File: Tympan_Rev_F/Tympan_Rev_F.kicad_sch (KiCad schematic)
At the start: 89 parts, among them J1 SJ-3523-SMT-TR, J2 SJ-3524-SMT-TR-PI, J3 Conn_01x06, J4 Qwiik Connector, J7 J-Link, P1 CONN_01X06, P2 CONN_01X06, P3 CONN_01X06, P4 CONN_01X06, P6 CONN_01X01, P7 CONN_01X01, P8 CONN_01X01, SW1 CL-SB-22A, SW2 SW_Push, U1 MCP73831, U2 TLV320AIC3206IRSBT, U3 74LVC1G66, U4 LP5907MFX-1.8, U5 Teensy4.1, U6 LC709203, U7 MDBT50Q-1MV2, Y1 32.768

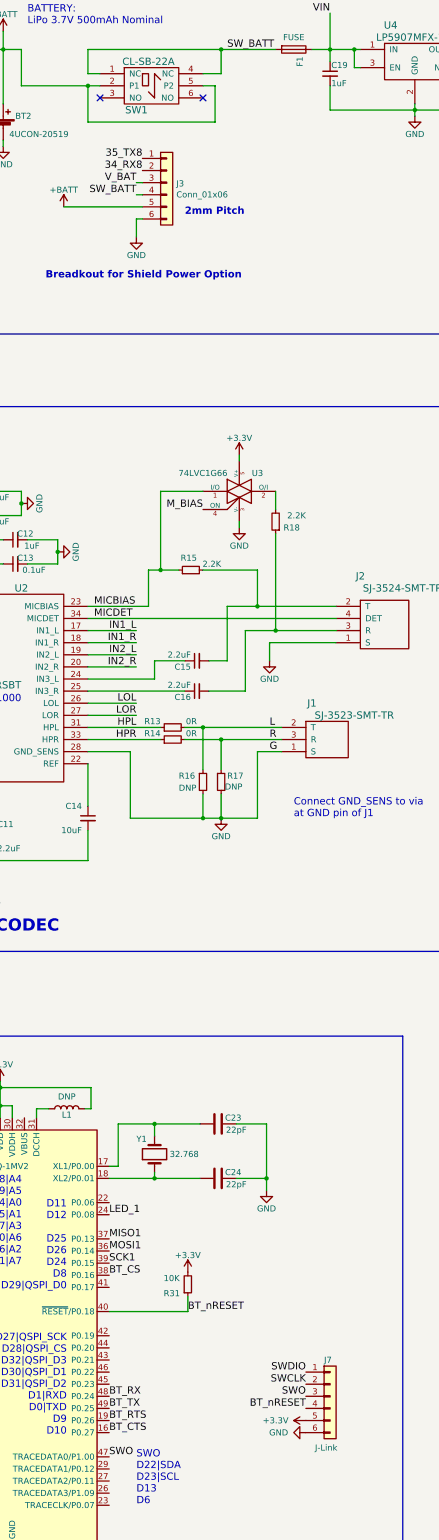
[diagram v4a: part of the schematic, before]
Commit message: first pass at laying out the J-Link interface
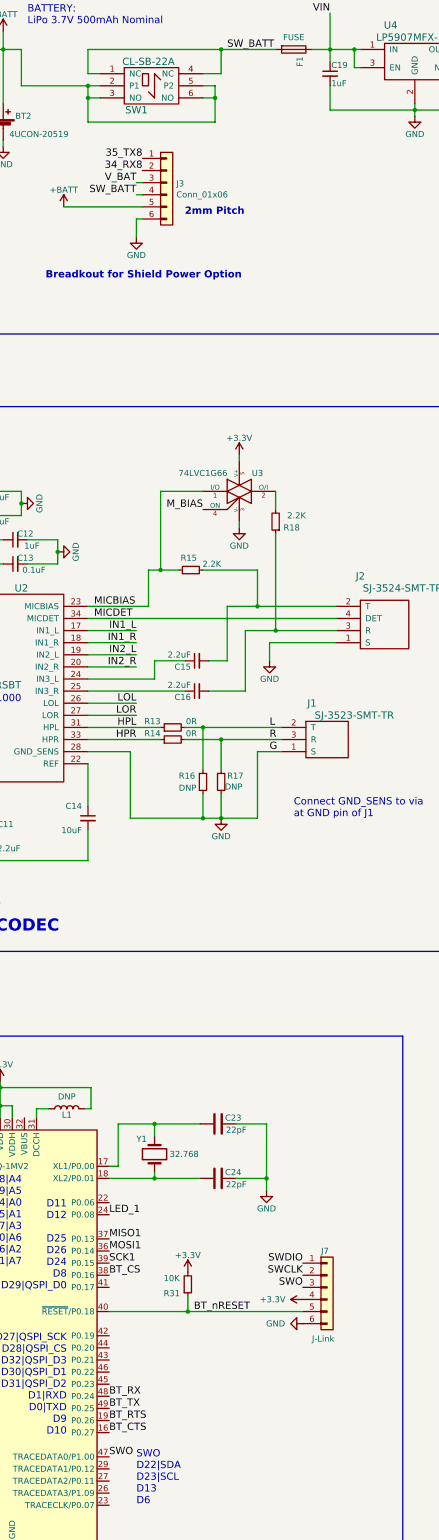
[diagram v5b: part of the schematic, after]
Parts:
- J7: footprint Connector_PinHeader_2.54mm:PinHeader_2x03_P2.54mm_Vertical_SMD -> Solutions:J-Link_SMT_SIP_0.1inP
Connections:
- net +3.3V: now also J7.4 (Pin_4); no longer J7.5 (Pin_5)
- net +BATT: now also SW1.3 (NO), SW1.6 (NO)
- net BT_nRESET: now also J7.5 (Pin_5); no longer J7.4 (Pin_4)
- no-connect marks 4 -> 2
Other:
- moved on the sheet: J7
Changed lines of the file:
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@@
     (rev "v1")
     (company "Tympan Master Hearing Aid Project")
-    (comment 1 "Designed by Flywheel Lab, Brooklyn")
+    (comment 1 "Designed by Flywheel Lab, Troy")
   )
   (junction (at 109.22 215.9) (diameter 0) (color 0 0 0 0)
@@
   (junction (at 189.23 54.61) (diameter 0) (color 0 0 0 0)
   )
+  (junction (at 160.02 64.77) (diameter 0) (color 0 0 0 0)
+  )
   (junction (at 261.62 152.4) (diameter 0) (color 0 0 0 0)
   )
@@
   (junction (at 114.935 276.225) (diameter 0) (color 0 0 0 0)
   )
+  (junction (at 133.35 64.77) (diameter 0) (color 0 0 0 0)
+  )
   (junction (at 114.935 272.415) (diameter 0) (color 0 0 0 0)
   )
@@
   (junction (at 96.52 142.24) (diameter 0) (color 0 0 0 0)
   )
+  (junction (at 154.305 319.405) (diameter 0) (color 0 0 0 0)
+  )
   (junction (at 219.71 54.61) (diameter 0) (color 0 0 0 0)
   )
@@
   )
   (no_connect (at 288.29 196.85))
-  (no_connect (at 157.48 64.77))
   (no_connect (at 288.29 162.56))
-  (no_connect (at 135.89 64.77))
   (wire (pts (xy 97.79 213.36) (xy 97.79 215.9))
     (stroke (width 0) (type default))
@@
     (stroke (width 0) (type default))
   )
-  (wire (pts (xy 133.35 62.23) (xy 133.35 69.85))
+  (wire (pts (xy 133.35 62.23) (xy 133.35 64.77))
     (stroke (width 0) (type default))
   )
@@
     (stroke (width 0) (type default))
   )
-  (wire (pts (xy 160.02 62.23) (xy 160.02 69.85))
+  (wire (pts (xy 160.02 62.23) (xy 160.02 64.77))
     (stroke (width 0) (type default))
   )
@@
     (stroke (width 0) (type default))
   )
+  (wire (pts (xy 133.35 64.77) (xy 135.89 64.77))
+    (stroke (width 0) (type default))
+  )
   (wire (pts (xy 261.62 190.5) (xy 264.16 190.5))
     (stroke (width 0) (type default))
@@
     (stroke (width 0) (type default))
   )
+  (wire (pts (xy 160.02 64.77) (xy 160.02 69.85))
+    (stroke (width 0) (type default))
+  )
+  (wire (pts (xy 157.48 64.77) (xy 160.02 64.77))
+    (stroke (width 0) (type default))
+  )
   (wire (pts (xy 426.085 150.495) (xy 445.135 150.495))
     (stroke (width 0) (type default))
@@
     (stroke (width 0) (type default))
   )
+  (wire (pts (xy 133.35 64.77) (xy 133.35 69.85))
+    (stroke (width 0) (type default))
+  )
   (wire (pts (xy 262.89 59.69) (xy 262.89 60.96))
     (stroke (width 0) (type default))
@@
     (stroke (width 0) (type default))
   )
+  (wire (pts (xy 137.795 319.405) (xy 154.305 319.405))
+    (stroke (width 0) (type default))
+  )
   (polyline (pts (xy 234.95 31.75) (xy 31.75 31.75))
     (stroke (width 0) (type default))
@@
     (stroke (width 0) (type default))
   )
-  (wire (pts (xy 137.795 319.405) (xy 154.305 319.405))
-    (stroke (width 0) (type default))
-  )
   (wire (pts (xy 164.465 280.035) (xy 170.815 280.035))
     (stroke (width 0) (type default))
@@
     (stroke (width 0) (type default))
   )
+  (wire (pts (xy 154.305 319.405) (xy 178.435 319.405))
+    (stroke (width 0) (type default))
+  )
   (wire (pts (xy 77.47 201.93) (xy 69.85 201.93))
     (stroke (width 0) (type default))
@@
     (effects (font (size 1.524 1.524)) (justify right bottom))
   )
-  (label "SWO" (at 179.07 337.185 180) (fields_autoplaced)
+  (label "SWO" (at 178.435 314.325 180) (fields_autoplaced)
     (effects (font (size 1.524 1.524)) (justify right bottom))
   )
-  (label "SWDIO" (at 179.07 332.105 180) (fields_autoplaced)
+  (label "SWDIO" (at 178.435 309.245 180) (fields_autoplaced)
     (effects (font (size 1.524 1.524)) (justify right bottom))
   )
@@
     (effects (font (size 1.524 1.524)) (justify right bottom))
   )
-  (label "SWCLK" (at 179.07 334.645 180) (fields_autoplaced)
+  (label "SWCLK" (at 178.435 311.785 180) (fields_autoplaced)
     (effects (font (size 1.524 1.524)) (justify right bottom))
   )
@@
     (effects (font (size 1.524 1.524)) (justify left bottom))
   )
-  (label "BT_nRESET" (at 154.305 319.405 0) (fields_autoplaced)
+  (label "BT_nRESET" (at 155.575 319.405 0) (fields_autoplaced)
     (effects (font (size 1.524 1.524)) (justify left bottom))
   )
@@
     (effects (font (size 1.524 1.524)) (justify left bottom))
   )
-  (label "BT_nRESET" (at 179.07 339.725 180) (fields_autoplaced)
-    (effects (font (size 1.524 1.524)) (justify right bottom))
-  )
   (label "SDA" (at 450.215 78.105 0) (fields_autoplaced)
     (effects (font (size 1.524 1.524)) (justify left bottom))
@@
     )
   )
-  (symbol (lib_id "power:GND") (at 179.07 344.805 270) (unit 1)
+  (symbol (lib_id "power:GND") (at 178.435 321.945 270) (unit 1)
     (in_bom yes) (on_board yes) (dnp no)
-    (property "Reference" "#PWR04" (at 172.72 344.805 0)
+    (property "Reference" "#PWR04" (at 172.085 321.945 0)
       (effects (font (size 1.27 1.27)) hide)
     )
-    (property "Value" "GND" (at 173.355 344.805 90)
+    (property "Value" "GND" (at 172.72 321.945 90)
       (effects (font (size 1.27 1.27)))
     )
-    (property "Footprint" "" (at 179.07 344.805 0)
+    (property "Footprint" "" (at 178.435 321.945 0)
       (effects (font (size 1.27 1.27)))
     )
-    (property "Datasheet" "" (at 179.07 344.805 0)
+    (property "Datasheet" "" (at 178.435 321.945 0)
       (effects (font (size 1.27 1.27)))
     )
@@
     )
   )
-  (symbol (lib_id "power:+3.3V") (at 179.07 342.265 90) (unit 1)
+  (symbol (lib_id "power:+3.3V") (at 178.435 316.865 90) (unit 1)
     (in_bom yes) (on_board yes) (dnp no)
-    (property "Reference" "#PWR03" (at 182.88 342.265 0)
+    (property "Reference" "#PWR03" (at 182.245 316.865 0)
       (effects (font (size 1.27 1.27)) hide)
     )
-    (property "Value" "+3.3V" (at 172.72 342.265 90)
+    (property "Value" "+3.3V" (at 172.085 316.865 90)
       (effects (font (size 1.27 1.27)))
     )
-    (property "Footprint" "" (at 179.07 342.265 0)
+    (property "Footprint" "" (at 178.435 316.865 0)
       (effects (font (size 1.27 1.27)))
     )
-    (property "Datasheet" "" (at 179.07 342.265 0)
+    (property "Datasheet" "" (at 178.435 316.865 0)
       (effects (font (size 1.27 1.27)))
     )
@@
     )
   )
-  (symbol (lib_id "Connector_Generic:Conn_01x06") (at 184.15 337.185 0) (unit 1)
+  (symbol (lib_id "Connector_Generic:Conn_01x06") (at 183.515 314.325 0) (unit 1)
     (in_bom yes) (on_board yes) (dnp no)
-    (property "Reference" "J7" (at 182.88 329.565 0)
+    (property "Reference" "J7" (at 182.245 306.705 0)
       (effects (font (size 1.27 1.27)) (justify left))
     )
-    (property "Value" "J-Link" (at 180.975 347.98 0)
+    (property "Value" "J-Link" (at 180.34 325.12 0)
       (effects (font (size 1.27 1.27)) (justify left))
     )
-    (property "Footprint" "Connector_PinHeader_2.54mm:PinHeader_2x03_P2.54mm_Vertical_SMD" (at 184.15 337.185 0)
+    (property "Footprint" "Solutions:J-Link_SMT_SIP_0.1inP" (at 183.515 314.325 0)
       (effects (font (size 1.27 1.27)) hide)
     )
-    (property "Datasheet" "~" (at 184.15 337.185 0)
+    (property "Datasheet" "~" (at 183.515 314.325 0)
       (effects (font (size 1.27 1.27)) hide)
     )

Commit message: Production Files Approved
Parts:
- D2: value LED -> RED LED
- D3: value LED -> GREEN LED
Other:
- note removed: "GREEN"
- note removed: "RED"
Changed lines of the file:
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@@
     (effects (font (size 1.524 1.524)) (justify left bottom))
-  )
-  (text "GREEN" (at 449.58 213.995 90)
-    (effects (font (size 1.524 1.524)) (justify right bottom))
   )
   (text "GAS GUAGE\nI2C ADDRESS 0001011\nUSE INTERNAL PULLUP ON ALARMB PIN"
@@
   (text "APHB1608CGKSEKC\nReplacement" (at 43.18 81.28 0)
     (effects (font (size 1.524 1.524)) (justify left bottom))
-  )
-  (text "RED" (at 435.61 213.995 90)
-    (effects (font (size 1.524 1.524)) (justify right bottom))
   )
   (text "CW\n\n\n\n\nCCW" (at 461.01 213.995 0)
@@
       (effects (font (size 1.27 1.27)))
     )
-    (property "Value" "LED" (at 431.8 215.265 0)
+    (property "Value" "RED LED" (at 433.07 215.265 0)
       (effects (font (size 1.27 1.27)))
     )
@@
       (effects (font (size 1.27 1.27)))
     )
-    (property "Value" "LED" (at 445.77 215.265 0)
-      (effects (font (size 1.27 1.27)))
-    )
+    (property "Value" "GREEN LED" (at 447.04 215.265 0)
+      (effects (font (size 1.27 1.27)))
+    )

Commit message: Update schematic pdf
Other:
- note added: "GAS GUAGE I2C ADDRESS 0001011 USE INTERNAL PULLUP ON ALARMB PIN PART IS UNAVAILABLE AT BUILD DATE! NOT POPULATED"
- note added: "Same pin out and orientation as Rev D & Rev E for compatibility with Shields"
- note removed: "GAS GUAGE I2C ADDRESS 0001011 USE INTERNAL PULLUP ON ALARMB PIN"
- note removed: "Removed P5 because it does not fit on board"
- note removed: "Same pin out and orientation as Rev D for compatibility with Shields"
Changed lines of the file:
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@@
   (title_block
     (title "Tympan Rev F")
-    (date "2024-01-19")
+    (date "2024-03-25")
     (rev "v1")
     (company "Tympan Master Hearing Aid Project")
-    (comment 1 "Designed by Flywheel Lab, Troy")
+    (comment 1 "Designed by Flywheel Lab, Troy NY")
   )
   (junction (at 109.22 215.9) (diameter 0) (color 0 0 0 0)
@@
     (effects (font (size 1.524 1.524)) (justify left bottom))
   )
-  (text "Same pin out and orientation as Rev D\nfor compatibility with Shields"
-    (at 256.54 290.83 0)
+  (text "Same pin out and orientation as Rev D & Rev E\nfor compatibility with Shields"
+    (at 249.555 290.83 0)
     (effects (font (size 2.54 2.54)) (justify left bottom))
   )
@@
     (effects (font (size 1.524 1.524)) (justify left bottom))
   )
-  (text "GAS GUAGE\nI2C ADDRESS 0001011\nUSE INTERNAL PULLUP ON ALARMB PIN"
-    (at 256.54 78.74 0)
+  (text "GAS GUAGE\nI2C ADDRESS 0001011\nUSE INTERNAL PULLUP ON ALARMB PIN\n\nPART IS UNAVAILABLE AT BUILD DATE!\nNOT POPULATED"
+    (at 247.396 84.328 0)
     (effects (font (size 1.524 1.524)) (justify left bottom))
   )
@@
     (effects (font (size 1.524 1.524) (thickness 0.3048) bold) (justify left bottom))
   )
-  (text "Removed P5 because it does not fit on board" (at 401.955 292.1 0)
-    (effects (font (size 1.524 1.524)) (justify left bottom))
-  )
   (text "MJTP-1117" (at 443.865 154.305 0)
